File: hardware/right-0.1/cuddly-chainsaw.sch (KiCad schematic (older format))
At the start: 92 parts, among them J1 USB_C_Receptacle_USB2.0, J2 USB_C_Receptacle_USB2.0, SW1 Encoder_MX_RGB, SW10 MX_RGB, SW11 MX_RGB, SW12 MX_RGB, SW13 MX_RGB, SW14 MX_RGB, SW15 MX_RGB, SW16 MX_RGB, SW17 MX_RGB, SW18 MX_RGB, SW19 MX_RGB, SW2 MX_RGB, SW20 MX_RGB, SW21 MX_RGB, SW22 MX_RGB, SW23 MX_RGB, SW24 MX_RGB, SW25 MX_RGB, SW26 MX_RGB, SW27 MX_RGB, SW28 MX_RGB, SW29 MX_RGB, SW3 MX_RGB, SW30 MX_RGB, SW31 MX_RGB, SW32 MX_RGB, SW33 MX_RGB, SW34 MX_RGB, SW36 MX_RGB, SW37 MX_RGB, SW38 MX_RGB, SW39 MX_RGB, SW4 MX_RGB, SW40 MX_RGB, SW41 MX_RGB, SW42 MX_RGB, SW5 MX_RGB, SW6 MX_RGB, SW7 MX_RGB, SW8 MX_RGB, SW9 MX_RGB, U1 USBLC6-2SC6

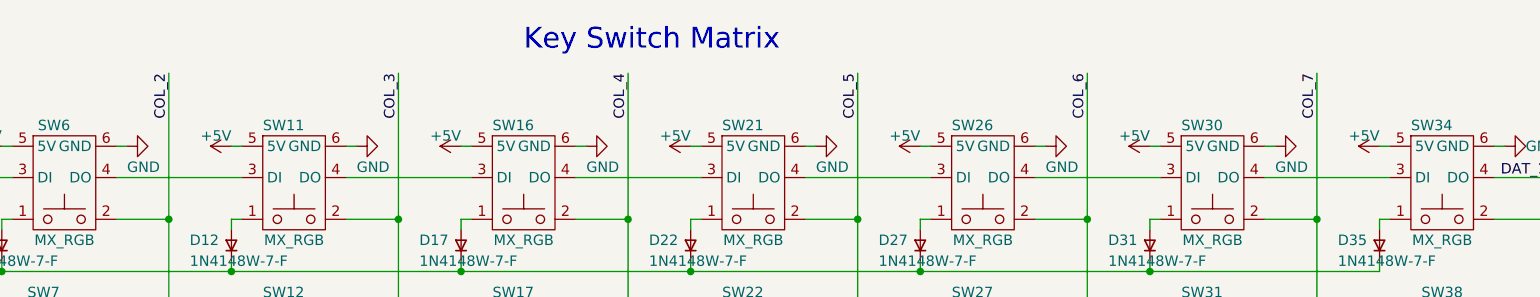
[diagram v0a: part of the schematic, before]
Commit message: first go at board outline done
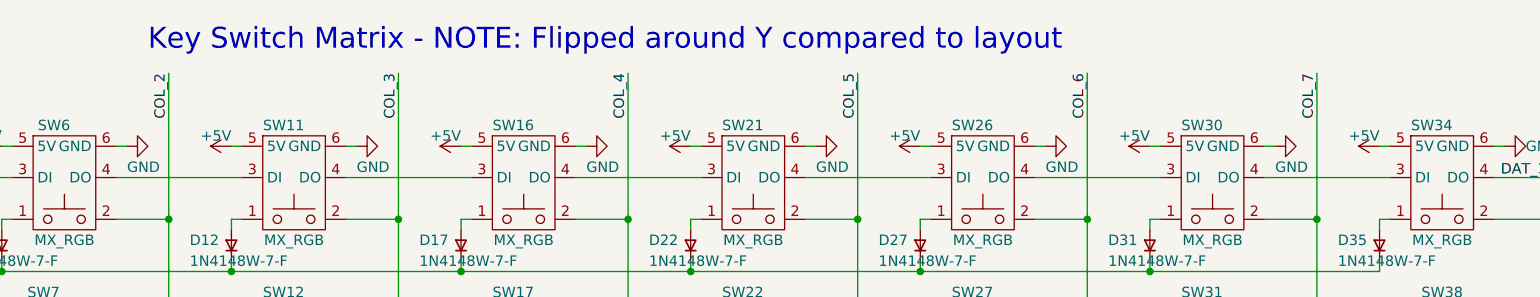
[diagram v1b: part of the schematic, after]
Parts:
- SW14: footprint josh-buttons-switches:MX_KEYSWITCH_RGB -> josh-buttons-switches:MX_KEYSWITCH_RGB_1.75U
- SW37: footprint josh-buttons-switches:MX_KEYSWITCH_RGB -> josh-buttons-switches:MX_KEYSWITCH_RGB_2.5U
- SW6: footprint josh-buttons-switches:MX_KEYSWITCH_RGB -> josh-buttons-switches:MX_KEYSWITCH_RGB_2U
- SW7: footprint josh-buttons-switches:MX_KEYSWITCH_RGB -> josh-buttons-switches:MX_KEYSWITCH_RGB_1.5U
- SW8: footprint josh-buttons-switches:MX_KEYSWITCH_RGB -> josh-buttons-switches:MX_KEYSWITCH_RGB_2.25U
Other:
- note added: "Key Switch Matrix - NOTE: Flipped around Y compared to layout"
- note removed: "Key Switch Matrix"
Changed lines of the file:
@@
 F 0 "SW37" H 8050 5000 50  0000 C CNN
 F 1 "MX_RGB" H 8100 4450 50  0000 C CNN
-F 2 "josh-buttons-switches:MX_KEYSWITCH_RGB" H 8100 4750 50  0001 C CNN
+F 2 "josh-buttons-switches:MX_KEYSWITCH_RGB_2.5U" H 8100 4750 50  0001 C CNN
 F 3 "~" H 8100 4750 50  0001 C CNN
 F 4 "DNP" H 8100 4550 50  0001 C CNN "DNP"
@@
 F 0 "SW7" H 2500 2750 50  0000 C CNN
 F 1 "MX_RGB" H 2600 2200 50  0000 C CNN
-F 2 "josh-buttons-switches:MX_KEYSWITCH_RGB" H 2600 2500 50  0001 C CNN
+F 2 "josh-buttons-switches:MX_KEYSWITCH_RGB_1.5U" H 2600 2500 50  0001 C CNN
 F 3 "~" H 2600 2500 50  0001 C CNN
 F 4 "DNP" H 2600 2300 50  0001 C CNN "DNP"
@@
 F 0 "SW8" H 2550 3500 50  0000 C CNN
 F 1 "MX_RGB" H 2600 2950 50  0000 C CNN
-F 2 "josh-buttons-switches:MX_KEYSWITCH_RGB" H 2600 3250 50  0001 C CNN
+F 2 "josh-buttons-switches:MX_KEYSWITCH_RGB_2.25U" H 2600 3250 50  0001 C CNN
 F 3 "~" H 2600 3250 50  0001 C CNN
 F 4 "DNP" H 2600 3050 50  0001 C CNN "DNP"
@@
 F 0 "SW6" H 2550 1950 50  0000 C CNN
 F 1 "MX_RGB" H 2600 1400 50  0000 C CNN
-F 2 "josh-buttons-switches:MX_KEYSWITCH_RGB" H 2600 1700 50  0001 C CNN
+F 2 "josh-buttons-switches:MX_KEYSWITCH_RGB_2U" H 2600 1700 50  0001 C CNN
 F 3 "~" H 2600 1700 50  0001 C CNN
 F 4 "DNP" H 2600 1500 50  0001 C CNN "DNP"
@@
 F 0 "SW14" H 3650 4250 50  0000 C CNN
 F 1 "MX_RGB" H 3700 3700 50  0000 C CNN
-F 2 "josh-buttons-switches:MX_KEYSWITCH_RGB" H 3700 4000 50  0001 C CNN
+F 2 "josh-buttons-switches:MX_KEYSWITCH_RGB_1.75U" H 3700 4000 50  0001 C CNN
 F 3 "~" H 3700 4000 50  0001 C CNN
 F 4 "DNP" H 3700 3800 50  0001 C CNN "DNP"
@@
 Wire Wire Line
 	1100 1100 1150 1100
-Text Notes 4800 700  0    100  ~ 0
-Key Switch Matrix
+Text Notes 3000 700  0    100  ~ 0
+Key Switch Matrix - NOTE: Flipped around Y compared to layout
 Connection ~ 7800 4800
 Connection ~ 9750 3800

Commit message: left all connected
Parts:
- added R9: 22R, Resistor_SMD:R_0603_1608Metric, symbol Device:R
- SW37: footprint josh-buttons-switches:MX_KEYSWITCH_RGB_2.5U -> josh-buttons-switches:MX_KEYSWITCH_RGB_2.5U_REV_STABS
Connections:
- net labels added: LED_KEYS, LED_UNDER
- net labels removed: LED_DAT
- wire segments 468 -> 470
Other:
- note added: "Underglow"
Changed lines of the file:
@@
 $Descr A4 11693 8268
 encoding utf-8
-Sheet 1 2
+Sheet 1 3
 Title "RIGHT HALF"
 Date "2020-01-09"
@@
 Text Notes 4000 7000 0    100  ~ 0
 BUZZ BUZZ
-Text Label 4050 7150 0    50   ~ 0
+Text Label 3650 7150 0    50   ~ 0
 PIEZO
-Wire Wire Line
-	4050 7150 4350 7150
 $Comp
 L Connector:USB_C_Receptacle_USB2.0 J?
@@
 Wire Wire Line
 	9300 5400 9800 5400
-Text Label 8550 6250 0    50   ~ 0
+Text Label 8800 6150 0    50   ~ 0
 COL_9
 $Sheet
@@
 Text Notes 9800 4600 0    100  ~ 0
 Keyboard Brain
-Text Label 8050 5850 0    50   ~ 0
+Text Label 8300 5750 0    50   ~ 0
 ROW_1
-Text Label 8050 5950 0    50   ~ 0
+Text Label 8300 5850 0    50   ~ 0
 ROW_2
-Text Label 8050 6050 0    50   ~ 0
+Text Label 8300 5950 0    50   ~ 0
 ROW_3
-Text Label 8050 6150 0    50   ~ 0
+Text Label 8300 6050 0    50   ~ 0
 ROW_4
-Text Label 8050 6250 0    50   ~ 0
+Text Label 8300 6150 0    50   ~ 0
 ROW_5
-Text Label 8550 5450 0    50   ~ 0
+Text Label 8800 5350 0    50   ~ 0
 COL_1
-Text Label 8550 5550 0    50   ~ 0
+Text Label 8800 5450 0    50   ~ 0
 COL_2
-Text Label 8550 5650 0    50   ~ 0
+Text Label 8800 5550 0    50   ~ 0
 COL_3
-Text Label 8550 5750 0    50   ~ 0
+Text Label 8800 5650 0    50   ~ 0
 COL_4
-Text Label 8550 5850 0    50   ~ 0
+Text Label 8800 5750 0    50   ~ 0
 COL_5
-Text Label 8550 5950 0    50   ~ 0
+Text Label 8800 5850 0    50   ~ 0
 COL_6
-Text Label 8550 6050 0    50   ~ 0
+Text Label 8800 5950 0    50   ~ 0
 COL_7
-Text Label 8550 6150 0    50   ~ 0
+Text Label 8800 6050 0    50   ~ 0
 COL_8
 Text Label 9300 5200 0    50   ~ 0
 SCL_SERIAL
-Text Label 8050 5450 0    50   ~ 0
-LED_DAT
-Text Label 8050 5550 0    50   ~ 0
+Text Label 8300 5350 0    50   ~ 0
+LED_KEYS
+Text Label 8300 5450 0    50   ~ 0
 PIEZO
-Text Label 8050 5650 0    50   ~ 0
+Text Label 8300 5550 0    50   ~ 0
 ENC_A
-Text Label 8050 5750 0    50   ~ 0
+Text Label 8300 5650 0    50   ~ 0
 ENC_B
 Wire Wire Line
@@
 F 0 "SW37" H 8050 5000 50  0000 C CNN
 F 1 "MX_RGB" H 8100 4450 50  0000 C CNN
-F 2 "josh-buttons-switches:MX_KEYSWITCH_RGB_2.5U" H 8100 4750 50  0001 C CNN
+F 2 "josh-buttons-switches:MX_KEYSWITCH_RGB_2.5U_REV_STABS" H 8100 4750 50  0001 C CNN
 F 3 "~" H 8100 4750 50  0001 C CNN
 F 4 "DNP" H 8100 4550 50  0001 C CNN "DNP"
@@
 Text Label 600  1300 0    50   ~ 0
 ENC_A
-Text Label 600  1200 0    50   ~ 0
-LED_DAT
 Wire Wire Line
 	600  1200 1150 1200
@@
 Connection ~ 9750 3050
 Connection ~ 9750 2300
+Text Label 8300 5250 0    50   ~ 0
+LED_UNDER
+Text Label 600  1200 0    50   ~ 0
+LED_KEYS
+$Comp
+L Device:R R9
+U 1 1 5E28FCCD
+P 4150 7150
+F 0 "R9" V 4050 7150 50  0000 C CNN
+F 1 "22R" V 4150 7150 50  0000 C CNN
+F 2 "Resistor_SMD:R_0603_1608Metric" V 4080 7150 50  0001 C CNN
+F 3 "~" H 4150 7150 50  0001 C CNN
+	1    4150 7150
+	0    1    1    0
+$EndComp
+Wire Wire Line
+	4300 7150 4350 7150
+Wire Wire Line
+	3650 7150 4000 7150
+$Sheet
+S 7350 6100 550  200
+U 5E330F76
+F0 "Leds" 100
+F1 "LEDs.sch" 100
+F2 "DIN" I L 7350 6200 50
+$EndSheet
+Text Label 7300 6200 2    50   ~ 0
+LED_UNDER
+Wire Wire Line
+	7300 6200 7350 6200
+Text Notes 7250 5900 0    100  ~ 0
+Underglow
 $EndSCHEMATC

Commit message: layout ++
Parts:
- SW1: DNP DNP -> (none); Digikey 987-1398-ND -> (none); LCSC C361165 -> (none); MPN EC11E1834403 -> (none)
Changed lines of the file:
@@
 $EndComp
 Wire Wire Line
-	4200 5700 4200 5650
+	4300 5850 4300 5800
 Connection ~ 4100 5850
 $Comp
 L power:+5V #PWR?
 U 1 1 5E189852
-P 4200 5650
+P 4300 5800
 AR Path="/5E16A0F8/5E189852" Ref="#PWR?"  Part="1"
 AR Path="/5E189852" Ref="#PWR0104"  Part="1"
-F 0 "#PWR0104" H 4200 5500 50  0001 C CNN
-F 1 "+5V" H 4215 5823 50  0000 C CNN
-F 2 "" H 4200 5650 50  0001 C CNN
-F 3 "" H 4200 5650 50  0001 C CNN
-	1    4200 5650
+F 0 "#PWR0104" H 4300 5650 50  0001 C CNN
+F 1 "+5V" H 4315 5973 50  0000 C CNN
+F 2 "" H 4300 5800 50  0001 C CNN
+F 3 "" H 4300 5800 50  0001 C CNN
+	1    4300 5800
 	1    0    0    -1
 $EndComp
@@
 	10650 1950 10600 1950
 $Comp
-L josh-keyboard:Encoder_MX_RGB SW1
-U 1 1 5E2B9951
-P 1450 1300
-F 0 "SW1" H 1350 1600 50  0000 C CNN
-F 1 "Encoder_MX_RGB" H 1450 1000 50  0000 C CNN
-F 2 "josh-buttons-switches:MX_KEYSWITCH_ENCODER_RGB" H 1300 1610 50  0001 C CNN
-F 3 "~" H 1450 1710 50  0001 C CNN
-F 4 "DNP" H 1450 1300 50  0001 C CNN "DNP"
-F 5 "987-1398-ND" H 1450 1300 50  0001 C CNN "Digikey"
-F 6 "C361165" H 1450 1300 50  0001 C CNN "LCSC"
-F 7 "EC11E1834403" H 1450 1300 50  0001 C CNN "MPN"
-	1    1450 1300
-	1    0    0    -1
-$EndComp
-$Comp
 L josh-keyboard:MX_RGB SW2
 U 1 1 5E2BA72B
@@
 Text Notes 7250 5900 0    100  ~ 0
 Underglow
+$Comp
+L josh-keyboard:Encoder_MX_RGB SW1
+U 1 1 5E260249
+P 1450 1300
+F 0 "SW1" H 1450 1725 50  0000 C CNN
+F 1 "Encoder_MX_RGB" H 1450 1634 50  0000 C CNN
+F 2 "josh-buttons-switches:MX_KEYSWITCH_ENCODER_RGB" H 1300 1610 50  0001 C CNN
+F 3 "~" H 1450 1710 50  0001 C CNN
+	1    1450 1300
+	1    0    0    -1
+$EndComp
 $EndSCHEMATC

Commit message: right half passes drc
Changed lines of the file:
@@
 Wire Wire Line
 	9300 5400 9800 5400
-Text Label 8800 6150 0    50   ~ 0
+Text Label 11050 4950 2    50   ~ 0
 COL_9
 $Sheet
@@
 Text Notes 9800 4600 0    100  ~ 0
 Keyboard Brain
-Text Label 8300 5750 0    50   ~ 0
-ROW_1
-Text Label 8300 5850 0    50   ~ 0
-ROW_2
-Text Label 8300 5950 0    50   ~ 0
-ROW_3
-Text Label 8300 6050 0    50   ~ 0
-ROW_4
-Text Label 8300 6150 0    50   ~ 0
-ROW_5
-Text Label 8800 5350 0    50   ~ 0
-COL_1
-Text Label 8800 5450 0    50   ~ 0
-COL_2
-Text Label 8800 5550 0    50   ~ 0
-COL_3
-Text Label 8800 5650 0    50   ~ 0
-COL_4
-Text Label 8800 5750 0    50   ~ 0
-COL_5
-Text Label 8800 5850 0    50   ~ 0
-COL_6
-Text Label 8800 5950 0    50   ~ 0
-COL_7
-Text Label 8800 6050 0    50   ~ 0
-COL_8
 Text Label 9300 5200 0    50   ~ 0
 SCL_SERIAL
-Text Label 8300 5350 0    50   ~ 0
-LED_KEYS
-Text Label 8300 5450 0    50   ~ 0
+Text Label 11050 5650 2    50   ~ 0
 PIEZO
-Text Label 8300 5550 0    50   ~ 0
+Text Label 11050 6000 2    50   ~ 0
 ENC_A
-Text Label 8300 5650 0    50   ~ 0
+Text Label 11050 5900 2    50   ~ 0
 ENC_B
 Wire Wire Line
@@
 Connection ~ 9750 3050
 Connection ~ 9750 2300
-Text Label 8300 5250 0    50   ~ 0
+Text Label 11050 5800 2    50   ~ 0
 LED_UNDER
 Text Label 600  1200 0    50   ~ 0
@@
 	1    0    0    -1
 $EndComp
+Text Label 9300 6000 0    50   ~ 0
+LED_KEYS
+Text Label 9300 6250 0    50   ~ 0
+ROW_4
+Text Label 11050 6300 2    50   ~ 0
+ROW_3
+Text Label 9300 5900 0    50   ~ 0
+COL_6
+Text Label 11050 5350 2    50   ~ 0
+COL_7
+Text Label 11050 5450 2    50   ~ 0
+COL_8
+Text Label 9300 6150 0    50   ~ 0
+ROW_5
+Text Label 9300 5800 0    50   ~ 0
+COL_5
+Text Label 9300 5600 0    50   ~ 0
+COL_4
+Text Label 9300 5400 0    50   ~ 0
+COL_1
+Text Label 9300 5500 0    50   ~ 0
+COL_2
+Text Label 9300 5700 0    50   ~ 0
+COL_3
+Text Label 11050 6200 2    50   ~ 0
+ROW_2
+Text Label 11050 6100 2    50   ~ 0
+ROW_1
 $EndSCHEMATC

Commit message: updated components due to jlk change
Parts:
- SW10, SW11, SW12, SW13, SW15, SW16, SW17, SW18, SW19, SW2, SW20, SW21, SW22, SW23, SW24, SW25, SW26, SW27, SW28, SW29, SW3, SW30, SW31, SW32, SW33, SW34, SW36, SW38, SW39, SW4, SW40, SW41, SW42, SW5, SW9: footprint josh-buttons-switches:MX_KEYSWITCH_RGB -> josh-keyboard:MX_KEYSWITCH_RGB
- SW14: footprint josh-buttons-switches:MX_KEYSWITCH_RGB_1.75U -> josh-keyboard:MX_KEYSWITCH_RGB_1.75U
- SW37: footprint josh-buttons-switches:MX_KEYSWITCH_RGB_2.5U_REV_STABS -> josh-keyboard:MX_KEYSWITCH_RGB_2.5U_REV_STABS
- SW6: footprint josh-buttons-switches:MX_KEYSWITCH_RGB_2U -> josh-keyboard:MX_KEYSWITCH_RGB_2U
- SW7: footprint josh-buttons-switches:MX_KEYSWITCH_RGB_1.5U -> josh-keyboard:MX_KEYSWITCH_RGB_1.5U
- SW8: footprint josh-buttons-switches:MX_KEYSWITCH_RGB_2.25U -> josh-keyboard:MX_KEYSWITCH_RGB_2.25U

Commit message: update board with new footprints
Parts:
- SW1: footprint josh-buttons-switches:MX_KEYSWITCH_ENCODER_RGB -> josh-keyboard:MX_KEYSWITCH_ENCODER_RGB
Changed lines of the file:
@@
 F 0 "SW1" H 1450 1725 50  0000 C CNN
 F 1 "Encoder_MX_RGB" H 1450 1634 50  0000 C CNN
-F 2 "josh-buttons-switches:MX_KEYSWITCH_ENCODER_RGB" H 1300 1610 50  0001 C CNN
+F 2 "josh-keyboard:MX_KEYSWITCH_ENCODER_RGB" H 1300 1610 50  0001 C CNN
 F 3 "~" H 1450 1710 50  0001 C CNN
 	1    1450 1300

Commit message: more layout
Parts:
- BZ1: DigiKey (none) -> 490-9647-1-ND; Digikey 490-9647-1-ND -> (none)
- D1, D10, D12, D13, D14, D15, D16, D17, D18, D19, D2, D20, D21, D22, D23, D24, D25, D26, D27, D28, D29, D3, D30, D31, D32, D33, D34, D35, D37, D38, D39, D4, D40, D41, D42, D43, D5, D6, D7, D8, D9: DigiKey (none) -> 1N4148W-FDICT-ND; Digikey 1N4148W-FDICT-ND -> (none)
- D11: DigiKey (none) -> SDM1100S1F-7DICT-ND; Digikey SDM1100S1F-7DICT-ND -> (none)
- F1: DigiKey (none) -> 507-1813-1-ND; Digikey 507-1813-1-ND -> (none)
- J1, J2: DigiKey (none) -> NA; Digikey NA -> (none)
- R1, R2: DigiKey (none) -> 118-CR0603-JW-512ELFCT-ND; Digikey 118-CR0603-JW-512ELFCT-ND -> (none)
- U1: DigiKey (none) -> 497-5235-1-ND; Digikey 497-5235-1-ND -> (none)
